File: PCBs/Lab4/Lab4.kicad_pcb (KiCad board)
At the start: 2 copper layers, 13 parts, among them IC1 M0C1103QDDFRQ1, J1 Conn_01x05_Pin, SW1 SW_SPST, SW2 SW_SPST

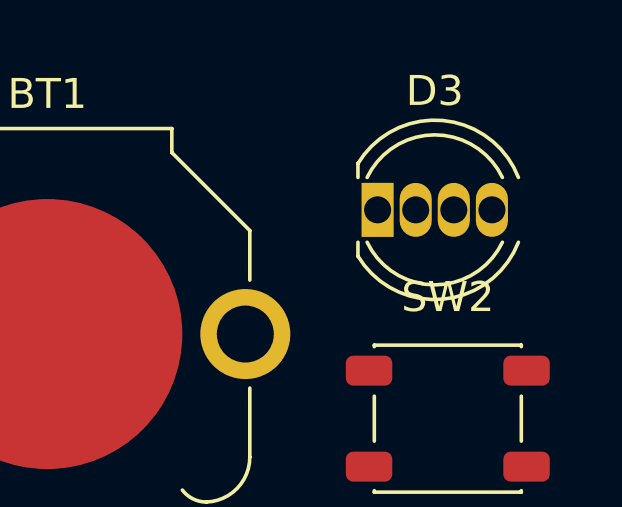
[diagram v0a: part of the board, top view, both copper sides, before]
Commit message: Switched through hole footprint for RGB LED
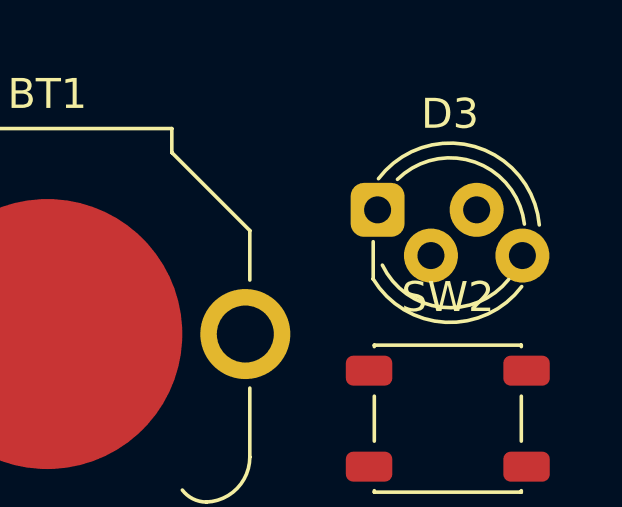
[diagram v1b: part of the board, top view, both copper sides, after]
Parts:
- D3: footprint LED_THT:LED_D5.0mm-4_RGB -> LED_THT:LED_D5.0mm-4_RGB_Staggered_Pins
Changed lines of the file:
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@@
 		)
 	)
-	(footprint "LED_THT:LED_D5.0mm-4_RGB"
+	(footprint "LED_THT:LED_D5.0mm-4_RGB_Staggered_Pins"
 		(layer "F.Cu")
 		(at 150.8325 88.69)
-		(descr "LED, RGB, diameter 5.0mm, 4 pins, https://www.kingbright.com/attachments/file/psearch/000/00/00/L-154A4SUREQBFZGEW(Ver.13A).pdf, generated by kicad-footprint-generator")
-		(tags "LED")
+		(descr "LED, diameter 5.0mm, 4 pins, WP154A4, https://www.kingbright.com/attachments/file/psearch/000/00/00/L-154A4SUREQBFZGEW(Ver.11A).pdf")
+		(tags "rgb led")
 		(property "Reference" "D3"
-			(at 1.905 -3.96 0)
+			(at 2.413 -3.198 0)
 			(layer "F.SilkS")
 			(effects
@@
 		)
 		(property "Value" "NeoPixel_THT"
-			(at 1.905 3.96 0)
+			(at 2.667 4.722 0)
 			(layer "F.Fab")
 			(effects
@@
 		(property "Datasheet" "https://www.adafruit.com/product/1938"
 			(at 0 0 0)
+			(unlocked yes)
 			(layer "F.Fab")
 			(hide yes)
@@
 		(property "Description" "RGB LED with integrated controller, 5mm/8mm LED package"
 			(at 0 0 0)
+			(unlocked yes)
 			(layer "F.Fab")
 			(hide yes)
@@
 		(attr through_hole)
 		(fp_line
-			(start -0.655 -1.545)
-			(end -0.655 -1.08)
-			(stroke
-				(width 0.12)
-				(type solid)
-			)
-			(layer "F.SilkS")
-		)
-		(fp_line
-			(start -0.655 1.08)
-			(end -0.655 1.545)
-			(stroke
-				(width 0.12)
-				(type solid)
-			)
-			(layer "F.SilkS")
-		)
-		(fp_arc
-			(start -0.655 -1.54483)
-			(mid 2.163898 -2.97877)
-			(end 4.693136 -1.08)
-			(stroke
-				(width 0.12)
-				(type solid)
-			)
-			(layer "F.SilkS")
-		)
-		(fp_arc
-			(start -0.349684 -1.08)
-			(mid 1.905 -2.5)
-			(end 4.159684 -1.08)
-			(stroke
-				(width 0.12)
-				(type solid)
-			)
-			(layer "F.SilkS")
-		)
-		(fp_arc
-			(start 4.159684 1.08)
-			(mid 1.905 2.5)
-			(end -0.349684 1.08)
-			(stroke
-				(width 0.12)
-				(type solid)
-			)
-			(layer "F.SilkS")
-		)
-		(fp_arc
-			(start 4.693136 1.08)
-			(mid 2.163898 2.97877)
-			(end -0.655 1.54483)
-			(stroke
-				(width 0.12)
-				(type solid)
-			)
-			(layer "F.SilkS")
-		)
-		(fp_line
-			(start -1.31 -3.21)
-			(end -1.31 3.21)
-			(stroke
-				(width 0.05)
-				(type solid)
-			)
-			(layer "F.CrtYd")
-		)
-		(fp_line
-			(start -1.31 3.21)
-			(end 5.12 3.21)
-			(stroke
-				(width 0.05)
-				(type solid)
-			)
-			(layer "F.CrtYd")
-		)
-		(fp_line
-			(start 5.12 -3.21)
-			(end -1.31 -3.21)
-			(stroke
-				(width 0.05)
-				(type solid)
-			)
-			(layer "F.CrtYd")
-		)
-		(fp_line
-			(start 5.12 3.21)
-			(end 5.12 -3.21)
-			(stroke
-				(width 0.05)
-				(type solid)
-			)
-			(layer "F.CrtYd")
-		)
-		(fp_line
-			(start -0.595 -1.469694)
-			(end -0.595 1.469694)
+			(start -0.147 1.061188)
+			(end -0.147 2.307)
+			(stroke
+				(width 0.12)
+				(type solid)
+			)
+			(layer "F.SilkS")
+		)
+		(fp_arc
+			(start 0.028 -1.038)
+			(mid 3.238737 -2.109652)
+			(end 5.389836 0.503784)
+			(stroke
+				(width 0.12)
+				(type solid)
+			)
+			(layer "F.SilkS")
+		)
+		(fp_arc
+			(start 0.660401 -1.015999)
+			(mid 3.242766 -1.592649)
+			(end 4.89309 0.475579)
+			(stroke
+				(width 0.12)
+				(type solid)
+			)
+			(layer "F.SilkS")
+		)
+		(fp_arc
+			(start 4.372086 2.315056)
+			(mid 2.134091 3.246393)
+			(end 0.158316 1.842)
+			(stroke
+				(width 0.12)
+				(type solid)
+			)
+			(layer "F.SilkS")
+		)
+		(fp_arc
+			(start 4.804334 2.556887)
+			(mid 2.262188 3.748194)
+			(end -0.147 2.30683)
+			(stroke
+				(width 0.12)
+				(type solid)
+			)
+			(layer "F.SilkS")
+		)
+		(fp_line
+			(start -1.02 -2.49)
+			(end 5.84 -2.49)
+			(stroke
+				(width 0.05)
+				(type solid)
+			)
+			(layer "F.CrtYd")
+		)
+		(fp_line
+			(start -1.02 4.01)
+			(end -1.02 -2.49)
+			(stroke
+				(width 0.05)
+				(type solid)
+			)
+			(layer "F.CrtYd")
+		)
+		(fp_line
+			(start 5.84 -2.49)
+			(end 5.84 4.01)
+			(stroke
+				(width 0.05)
+				(type solid)
+			)
+			(layer "F.CrtYd")
+		)
+		(fp_line
+			(start 5.84 4.01)
+			(end -1.02 4.01)
+			(stroke
+				(width 0.05)
+				(type solid)
+			)
+			(layer "F.CrtYd")
+		)
+		(fp_line
+			(start -0.087 -0.707694)
+			(end -0.087 2.231694)
 			(stroke
 				(width 0.1)
@@
 		)
 		(fp_arc
-			(start -0.595 -1.469694)
-			(mid 4.805 0)
-			(end -0.595 1.469694)
+			(start -0.087 -0.707694)
+			(mid 5.313 0.762016)
+			(end -0.087016 2.231666)
 			(stroke
 				(width 0.1)
@@
 		)
 		(fp_circle
-			(center 1.905 0)
-			(end 4.405 0)
+			(center 2.413 0.762)
+			(end 4.913 0.762)
 			(stroke
 				(width 0.1)
@@
 		)
 		(fp_text user "${REFERENCE}"
-			(at 1.905 0 0)
-			(layer "F.Fab")
-			(effects
-				(font
-					(size 0.8 0.8)
-					(thickness 0.12)
-				)
-			)
-		)
-		(pad "1" thru_hole rect
+			(at 2.413 -3.198 0)
+			(layer "F.Fab")
+			(effects
+				(font
+					(size 1 1)
+					(thickness 0.15)
+				)
+			)
+		)
+		(pad "1" thru_hole roundrect
 			(at 0 0)
-			(size 1.07 1.8)
-			(drill 0.9)
-			(layers "*.Cu" "*.Mask")
-			(remove_unused_layers no)
+			(size 1.8 1.8)
+			(drill 0.9)
+			(layers "*.Cu" "*.Mask")
+			(remove_unused_layers no)
+			(roundrect_rratio 0.25)
 			(net 6 "unconnected-(D3-DOUT-Pad1)")
 			(pinfunction "DOUT")
 			(pintype "output")
 		)
-		(pad "2" thru_hole oval
-			(at 1.27 0)
-			(size 1.07 1.8)
+		(pad "2" thru_hole circle
+			(at 1.778 1.524)
+			(size 1.8 1.8)
 			(drill 0.9)
 			(layers "*.Cu" "*.Mask")
@@
 			(pintype "power_in")
 		)
-		(pad "3" thru_hole oval
-			(at 2.54 0)
-			(size 1.07 1.8)
+		(pad "3" thru_hole circle
+			(at 3.302 0)
+			(size 1.8 1.8)
 			(drill 0.9)
 			(layers "*.Cu" "*.Mask")
@@
 			(pintype "power_in")
 		)
-		(pad "4" thru_hole oval
-			(at 3.81 0)
-			(size 1.07 1.8)
+		(pad "4" thru_hole circle
+			(at 4.826 1.524)
+			(size 1.8 1.8)
 			(drill 0.9)
 			(layers "*.Cu" "*.Mask")
@@
 		)
 		(embedded_fonts no)
-		(model "${KICAD9_3DMODEL_DIR}/LED_THT.3dshapes/LED_D5.0mm-4_RGB.step"
+		(model "${KICAD9_3DMODEL_DIR}/LED_THT.3dshapes/LED_D5.0mm-4_RGB_Staggered_Pins.step"
 			(offset
 				(xyz 0 0 0)
